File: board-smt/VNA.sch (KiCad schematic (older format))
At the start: 105 parts, among them J1 Conn_02x07_Odd_Even, J11 Conn_01x01, J13 Barrel_Jack, J14 Conn_01x01, J15 Conn_01x02, J16 Conn_01x01, J18 Conn_01x01, J19 Conn_01x01, J2 Conn_Coaxial, J20 Conn_01x01, J21 Conn_01x01, J24 USB_B, J3 Conn_01x01, J4 Conn_01x01, J5 Conn_01x01, J6 Conn_01x01, J7 Conn_01x01, J8 Conn_01x01, J9 Conn_Coaxial, Q3 S9018, SW1 SW_DPDT_x2, U1 SI5351A, U10 MT3608, U11 CN3052, U12 SI5351A, U8 AMS1117-3V3, U9 78M05_TO252, Y1 27 MHz

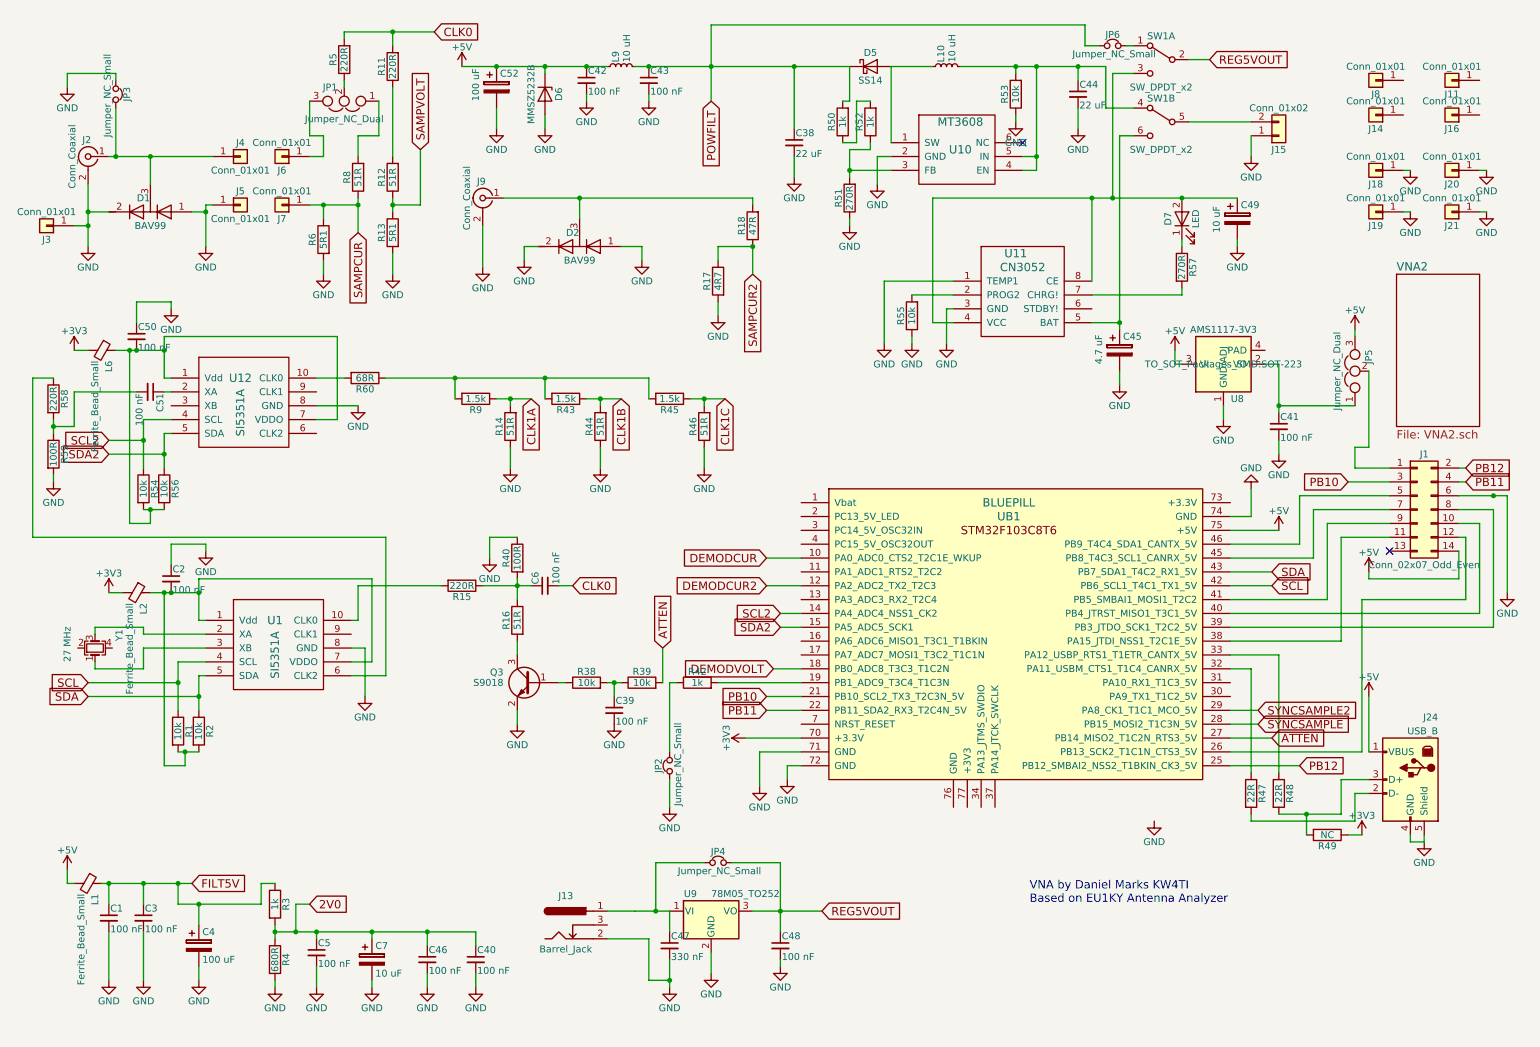
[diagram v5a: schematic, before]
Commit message: Bigger footprint for C4
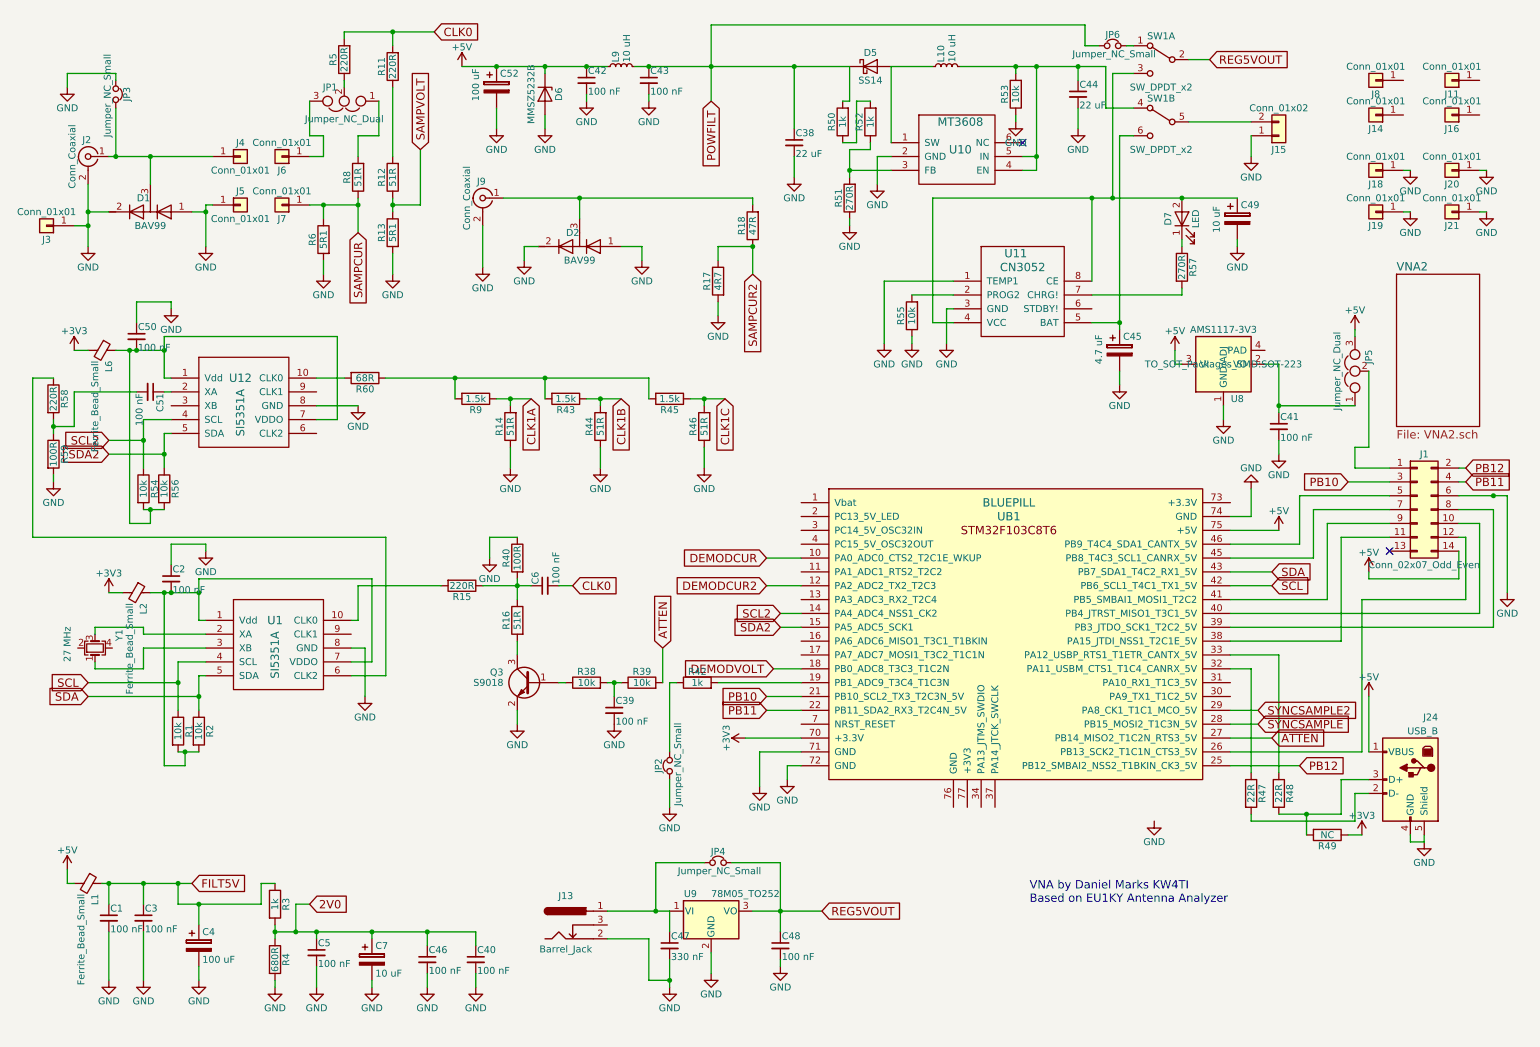
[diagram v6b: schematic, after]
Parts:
- C4: footprint Capacitors_SMD:CP_Elec_5x5.3 -> Capacitors_SMD:CP_Elec_8x10.5
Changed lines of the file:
@@
 F 0 "C4" H 1775 7300 50  0000 L CNN
 F 1 "100 uF" H 1775 7100 50  0000 L CNN
-F 2 "Capacitors_SMD:CP_Elec_5x5.3" H 1788 7050 50  0001 C CNN
+F 2 "Capacitors_SMD:CP_Elec_8x10.5" H 1788 7050 50  0001 C CNN
 F 3 "" H 1750 7200 50  0001 C CNN
 	1    1750 7200
@@
 Connection ~ 4550 850
 Wire Wire Line
-	3650 850  3900 850
-Wire Wire Line
-	3900 850  4250 850
-Wire Wire Line
-	4250 850  4550 850
-Wire Wire Line
-	4550 850  4700 850
+	3650 850  4700 850
 Wire Wire Line
 	4550 1100 4550 1050
 Connection ~ 5000 850
 Wire Wire Line
-	4900 850  5000 850
-Wire Wire Line
-	5000 850  5450 850
-Wire Wire Line
-	5450 850  6050 850
-Wire Wire Line
-	6050 850  6450 850
+	4900 850  6450 850
 Wire Wire Line
 	5000 1100 5000 1050
 Wire Wire Line
-	7250 850  7650 850
-Wire Wire Line
-	7650 850  7800 850
-Wire Wire Line
-	7800 850  8100 850
-Wire Wire Line
-	8100 850  8300 850
+	7250 850  8300 850
 Wire Wire Line
 	6750 850  7050 850
@@
 	6450 1600 6750 1600
 Wire Wire Line
-	6450 1450 6450 1600
-Wire Wire Line
-	6450 1600 6450 1650
+	6450 1450 6450 1650
 Wire Wire Line
 	6450 850  6450 1100
@@
 	7800 1500 7700 1500
 Wire Wire Line
-	7800 850  7800 1500
-Wire Wire Line
-	7800 1500 7800 1600
+	7800 850  7800 1600
 Wire Wire Line
 	6650 1500 6750 1500
@@
 	10000 6250 10000 6000
 Wire Wire Line
-	9550 6250 9750 6250
-Wire Wire Line
-	9750 6250 10000 6250
+	9550 6250 10000 6250
 Wire Wire Line
 	9550 5100 9550 5950
@@
 	5150 5300 5150 5800
 Wire Wire Line
-	3100 3100 3600 3100
-Wire Wire Line
-	3600 3100 4250 3100
-Wire Wire Line
-	4250 3100 5000 3100
+	3100 3100 5000 3100
 Wire Wire Line
 	3600 3250 3600 3100
@@
 	5400 3750 5400 3600
 Wire Wire Line
-	5300 3250 5400 3250
-Wire Wire Line
-	5400 3250 5550 3250
+	5300 3250 5550 3250
 Wire Wire Line
 	5400 3250 5400 3300
@@
 	4650 3750 4650 3600
 Wire Wire Line
-	4550 3250 4650 3250
-Wire Wire Line
-	4650 3250 4800 3250
+	4550 3250 4800 3250
 Wire Wire Line
 	4650 3250 4650 3300
@@
 	9550 3300 10100 3300
 Wire Wire Line
-	9550 3000 9550 3300
-Wire Wire Line
-	9550 3300 9550 3350
+	9550 3000 9550 3350
 Wire Wire Line
 	9450 3000 9550 3000
@@
 	5850 5500 6100 5500
 Wire Wire Line
-	10850 3950 11100 3950
-Wire Wire Line
-	11100 3950 11200 3950
+	10850 3950 11200 3950
 Wire Wire Line
 	10850 4050 11100 4050
@@
 	1350 5050 1800 5050
 Wire Wire Line
-	1750 4550 1750 4650
-Wire Wire Line
-	1750 4650 1750 4850
+	1750 4550 1750 4850
 Wire Wire Line
 	1750 4850 1800 4850
 Wire Wire Line
-	1600 5150 1600 5300
-Wire Wire Line
-	1600 5300 1600 5500
+	1600 5150 1600 5500
 Wire Wire Line
 	1600 5150 1800 5150
 Wire Wire Line
-	1750 5250 1750 5400
-Wire Wire Line
-	1750 5400 1750 5500
+	1750 5250 1750 5500
 Wire Wire Line
 	1750 5250 1800 5250
@@
 	800  6750 850  6750
 Wire Wire Line
-	1050 6750 1100 6750
-Wire Wire Line
-	1100 6750 1350 6750
-Wire Wire Line
-	1350 6750 1600 6750
-Wire Wire Line
-	1600 6750 1700 6750
+	1050 6750 1700 6750
 Wire Wire Line
 	1350 7100 1350 7450
@@
 	1100 4650 1200 4650
 Wire Wire Line
-	1400 4650 1500 4650
-Wire Wire Line
-	1500 4650 1550 4650
-Wire Wire Line
-	1550 4650 1750 4650
+	1400 4650 1750 4650
 Connection ~ 1550 4650
 Wire Wire Line
@@
 	2300 7450 2300 7500
 Wire Wire Line
-	2300 7050 2300 7100
-Wire Wire Line
-	2300 7100 2300 7150
+	2300 7050 2300 7150
 Wire Wire Line
 	1600 6750 1600 6900
 Wire Wire Line
-	1600 6900 1750 6900
-Wire Wire Line
-	1750 6900 2200 6900
+	1600 6900 2200 6900
 Wire Wire Line
 	2200 6900 2200 6750
@@
 Connection ~ 1600 6750
 Wire Wire Line
-	2300 7100 2450 7100
-Wire Wire Line
-	2450 7100 2600 7100
-Wire Wire Line
-	2600 7100 3000 7100
-Wire Wire Line
-	3000 7100 3400 7100
-Wire Wire Line
-	3400 7100 3750 7100
+	2300 7100 3750 7100
 Connection ~ 2300 7100
 Wire Wire Line
@@
 	4000 3750 4000 3600
 Wire Wire Line
-	3900 3250 4000 3250
-Wire Wire Line
-	4000 3250 4150 3250
+	3900 3250 4150 3250
 Wire Wire Line
 	4000 3250 4000 3300
@@
 	2900 4600 3500 4600
 Wire Wire Line
-	3800 4600 4050 4600
-Wire Wire Line
-	4050 4600 4150 4600
-Wire Wire Line
-	4050 4550 4050 4600
-Wire Wire Line
-	4050 4600 4050 4700
+	3800 4600 4150 4600
+Wire Wire Line
+	4050 4550 4050 4700
 Wire Wire Line
 	4050 5000 4050 5100
 Connection ~ 4050 4600
 Wire Wire Line
-	950  1700 950  1900
-Wire Wire Line
-	950  1900 950  2000
-Wire Wire Line
-	950  2000 950  2150
-Wire Wire Line
-	1100 1500 1150 1500
-Wire Wire Line
-	1150 1500 1400 1500
-Wire Wire Line
-	1400 1500 1850 1500
+	950  1700 950  2150
+Wire Wire Line
+	1100 1500 1850 1500
 Wire Wire Line
 	2650 2250 2650 2350
@@
 	2650 1950 2650 1850
 Wire Wire Line
-	2550 1850 2650 1850
-Wire Wire Line
-	2650 1850 2900 1850
-Wire Wire Line
-	2900 1800 2900 1850
-Wire Wire Line
-	2900 1850 2900 2050
+	2550 1850 2900 1850
+Wire Wire Line
+	2900 1800 2900 2050
 Connection ~ 2650 1850
 Connection ~ 2900 1850
@@
 	3150 700  3150 600
 Wire Wire Line
-	2800 600  3150 600
-Wire Wire Line
-	3150 600  3450 600
+	2800 600  3450 600
 Wire Wire Line
 	3150 1500 3150 1000
@@
 	3150 2350 3150 2200
 Wire Wire Line
-	3150 1800 3150 1850
-Wire Wire Line
-	3150 1850 3150 1900
+	3150 1800 3150 1900
 Wire Wire Line
 	3350 1450 3350 1850
@@
 	3800 2000 3800 2300
 Wire Wire Line
-	3950 1800 4500 1800
-Wire Wire Line
-	4500 1800 5750 1800
+	3950 1800 5750 1800
 Wire Wire Line
 	5500 2550 5500 2650
@@
 Connection ~ 1750 4650
 Wire Wire Line
-	1600 5800 1650 5800
-Wire Wire Line
-	1650 5800 1750 5800
+	1600 5800 1750 5800
 Wire Wire Line
 	1350 5200 1350 5050
@@
 	9200 5600 9400 5600
 Wire Wire Line
-	4700 6950 4900 6950
-Wire Wire Line
-	4900 6950 5050 6950
-Wire Wire Line
-	5050 6950 5150 6950
+	4700 6950 5150 6950
 Wire Wire Line
 	3400 7500 3400 7400
@@
 Connection ~ 5050 6950
 Wire Wire Line
-	5750 6950 5950 6950
-Wire Wire Line
-	5950 6950 6250 6950
-Wire Wire Line
-	5950 6600 5950 6950
-Wire Wire Line
-	5950 6950 5950 7100
+	5750 6950 6250 6950
+Wire Wire Line
+	5950 6600 5950 7100
 Wire Wire Line
 	5950 6600 5600 6600
 Connection ~ 5950 6950
 Wire Wire Line
-	5150 7300 5150 7450
-Wire Wire Line
-	5150 7450 5150 7500
+	5150 7300 5150 7500
 Wire Wire Line
 	5150 6950 5150 7100
@@
 	4400 5300 4350 5300
 Wire Wire Line
-	4700 5300 4750 5300
-Wire Wire Line
-	4750 5300 4800 5300
+	4700 5300 4800 5300
 Wire Wire Line
 	4750 5300 4750 5400
@@
 	8500 1350 8400 1350
 Wire Wire Line
-	8400 1350 8400 2700
-Wire Wire Line
-	8400 2700 8400 2750
+	8400 1350 8400 2750
 Wire Wire Line
 	8400 2700 8200 2700
@@
 	8500 900  8350 900
 Wire Wire Line
-	8350 900  8350 1800
+	8350 1800 8350 900
 Wire Wire Line
 	7050 1800 7050 2700
@@
 Connection ~ 8200 1800
 Wire Wire Line
-	7050 1800 8200 1800
-Wire Wire Line
-	8200 1800 8350 1800
-Wire Wire Line
-	8350 1800 8850 1800
-Wire Wire Line
-	8850 1800 9250 1800
+	7050 1800 9250 1800
 Connection ~ 8850 1800
 Wire Wire Line
@@
 	6700 2400 7200 2400
 Wire Wire Line
-	5450 550  5450 850
-Wire Wire Line
-	5450 850  5450 1100
+	5450 550  5450 1100
 Connection ~ 5450 850
 Wire Wire Line
@@
 Connection ~ 4250 3100
 Wire Wire Line
-	1500 2800 1500 2900
-Wire Wire Line
-	1500 2900 1500 3100
+	1500 2800 1500 3100
 Wire Wire Line
 	1500 3100 1550 3100
 Wire Wire Line
-	1350 3400 1350 3550
-Wire Wire Line
-	1350 3550 1350 3750
+	1350 3400 1350 3750
 Wire Wire Line
 	1350 3400 1550 3400
 Wire Wire Line
-	1500 3500 1500 3650
-Wire Wire Line
-	1500 3650 1500 3750
+	1500 3500 1500 3750
 Wire Wire Line
 	1500 3500 1550 3500
@@
 	850  2900 950  2900
 Wire Wire Line
-	1150 2900 1250 2900
-Wire Wire Line
-	1250 2900 1300 2900
-Wire Wire Line
-	1300 2900 1500 2900
+	1150 2900 1500 2900
 Connection ~ 1300 2900
 Wire Wire Line
@@
 Connection ~ 1500 2900
 Wire Wire Line
-	1350 4050 1400 4050
-Wire Wire Line
-	1400 4050 1500 4050
+	1350 4050 1500 4050
 Wire Wire Line
 	1400 4050 1400 4150
@@
 	1550 3200 1500 3200
 Wire Wire Line
-	700  3400 700  3450
-Wire Wire Line
-	700  3450 700  3500
+	700  3400 700  3500
 Wire Wire Line
 	1300 3200 850  3200
@@
 	4950 2150 4800 2150
 Wire Wire Line
-	1800 1850 1800 1900
-Wire Wire Line
-	1800 1900 1800 2150
+	1800 1850 1800 2150
 Wire Wire Line
 	1800 1850 1850 1850

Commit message: Updated Schematic
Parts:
- C4: value 100 uF -> 1000 uF
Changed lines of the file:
@@
 P 1750 7200
 F 0 "C4" H 1775 7300 50  0000 L CNN
-F 1 "100 uF" H 1775 7100 50  0000 L CNN
+F 1 "1000 uF" H 1775 7100 50  0000 L CNN
 F 2 "Capacitors_SMD:CP_Elec_8x10.5" H 1788 7050 50  0001 C CNN
 F 3 "" H 1750 7200 50  0001 C CNN

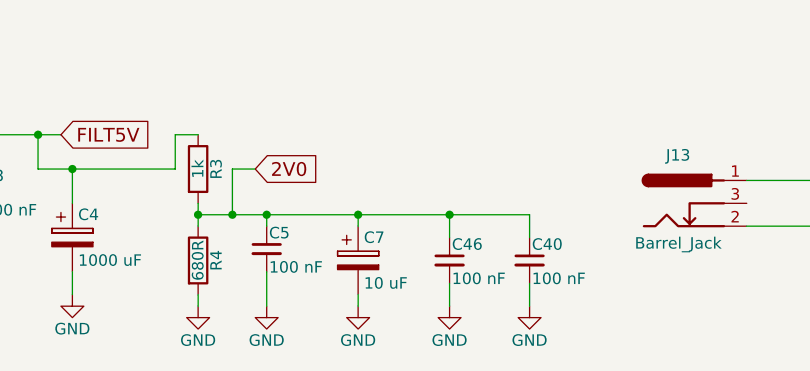
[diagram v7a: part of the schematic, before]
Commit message: Updated software to add cursor for smith chart, also changed edge of triggering
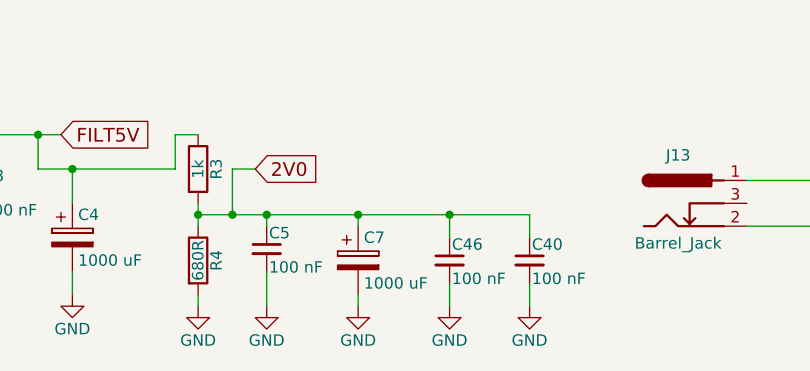
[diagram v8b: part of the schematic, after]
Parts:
- C7: value 10 uF -> 1000 uF; footprint Capacitors_SMD:CP_Elec_5x5.3 -> Capacitors_SMD:CP_Elec_8x10.5
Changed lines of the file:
@@
 P 3000 7300
 F 0 "C7" H 3025 7400 50  0000 L CNN
-F 1 "10 uF" H 3025 7200 50  0000 L CNN
-F 2 "Capacitors_SMD:CP_Elec_5x5.3" H 3038 7150 50  0001 C CNN
+F 1 "1000 uF" H 3025 7200 50  0000 L CNN
+F 2 "Capacitors_SMD:CP_Elec_8x10.5" H 3038 7150 50  0001 C CNN
 F 3 "" H 3000 7300 50  0001 C CNN
 	1    3000 7300
